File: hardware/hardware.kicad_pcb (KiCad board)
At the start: 2 copper layers, 100 x 100 mm, 129 parts, among them J1 Conn_01x04_Pin, J10 Conn_01x03, J11 AVR-ISP-6, J2 Conn_01x04_Pin, J3 Conn_01x04_Pin, J4 Conn_01x04_Pin, J5 Conn_01x04_Pin, J6 Conn_01x04_Pin, J7 Conn_01x04_Pin, J8 Conn_01x03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

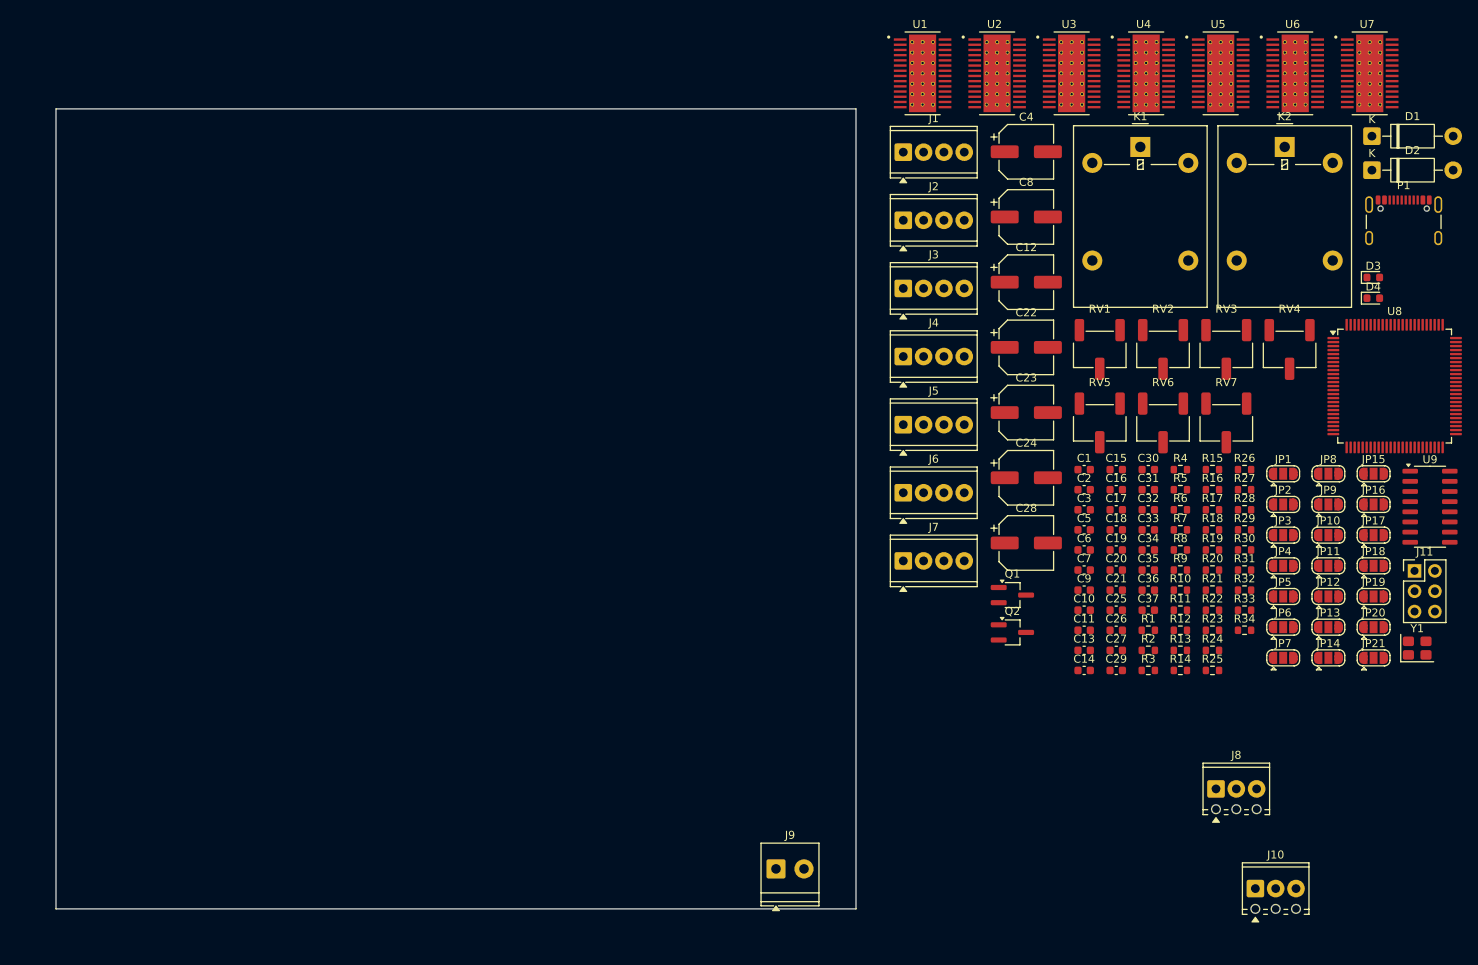
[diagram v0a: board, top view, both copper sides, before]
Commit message: placing relay + drv + edit relay footprints
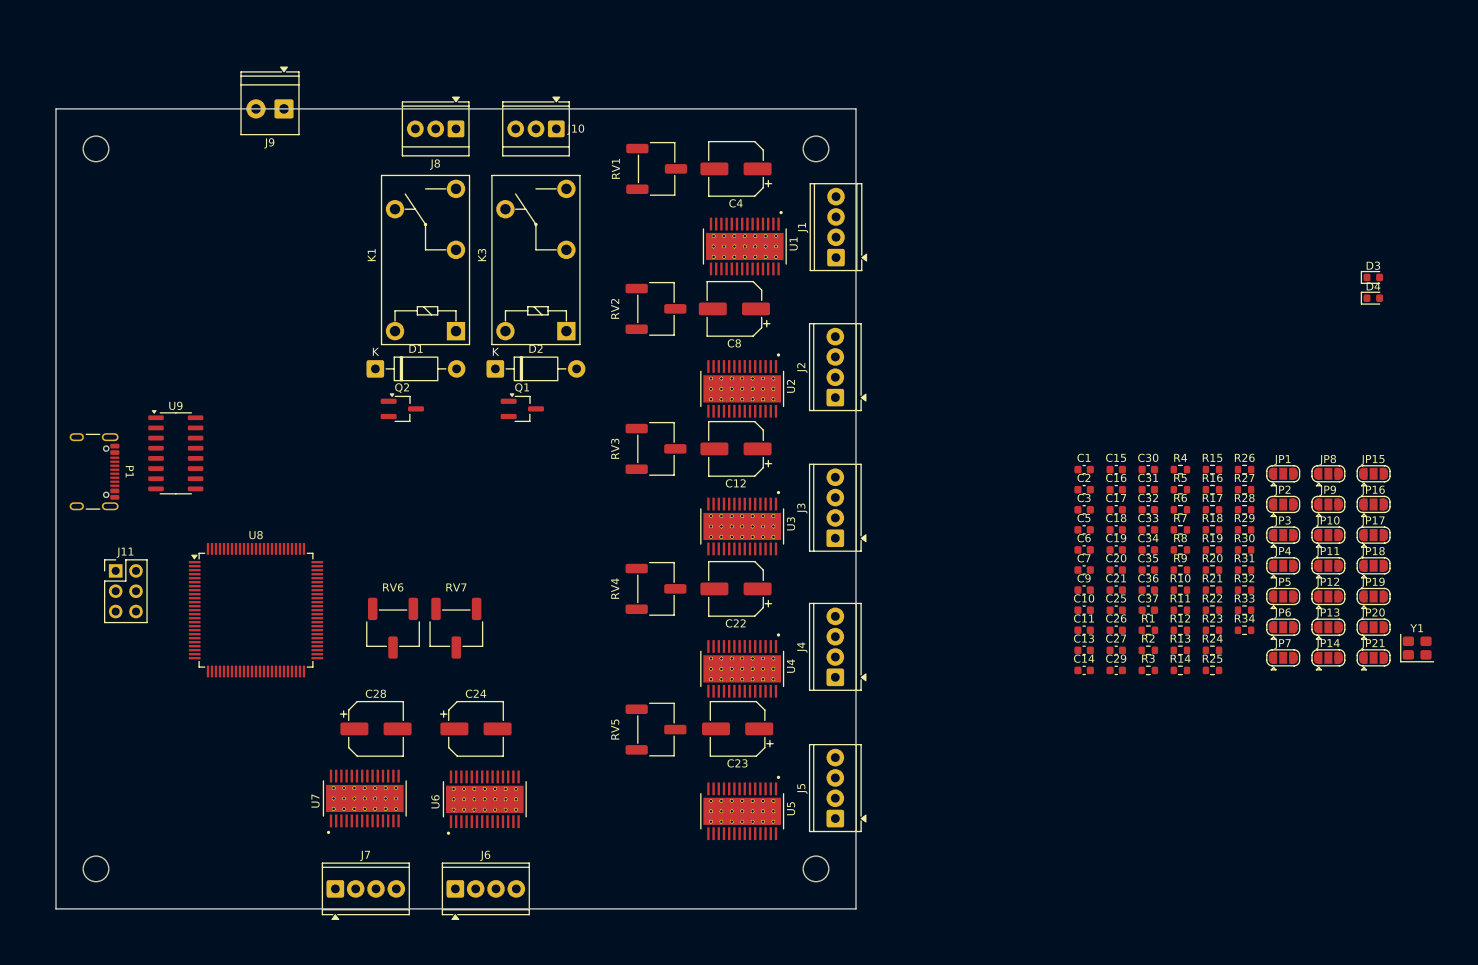
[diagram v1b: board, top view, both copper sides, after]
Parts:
- removed K2: RAYEX-L90, Relay_THT:Relay_SPDT_Omron-G5LE-1
- added K3: G5Q-1, Relay_THT:Relay_SPDT_Omron-G5Q-1, F.Cu at (113.8, 77.8)
- J10, J8: footprint TerminalBlock_Phoenix:TerminalBlock_Phoenix_MPT-0,5-3-2.54_1x03_P2.54mm_Horizontal -> TerminalBlock_TE-Connectivity:TerminalBlock_TE_282834-3_1x03_P2.54mm_Horizontal
- K1: value RAYEX-L90 -> G5Q-1; footprint Relay_THT:Relay_SPDT_Omron-G5LE-1 -> Relay_THT:Relay_SPDT_Omron-G5Q-1
- moved P1 167.5 mm to (53.7, 95.4), turned to -90 degrees
- moved J11 162.4 mm to (57.5, 107.8)
- moved U9 156.9 mm to (65.0, 93.1)
- moved U7 154.9 mm to (88.6, 136.2), turned to 90 degrees
- moved U8 145.1 mm to (75.0, 112.7)
- moved U6 136.0 mm to (103.6, 136.3), turned to 90 degrees
- moved J10 129.0 mm to (112.5, 52.5), turned to 180 degrees
- moved D1 127.9 mm to (89.9, 82.5)
- moved J8 125.8 mm to (100.0, 52.5), turned to 180 degrees
- moved J9 113.2 mm to (78.5, 50.0), turned to 180 degrees
- moved D2 112.4 mm to (104.9, 82.5)
- moved U5 109.9 mm to (135.8, 137.8), turned to -90 degrees
- moved RV6 99.6 mm to (92.1, 114.9)
- moved RV7 99.6 mm to (100.0, 114.9)
- moved U4 90.0 mm to (135.8, 120.0), turned to -90 degrees
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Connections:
- K1 pad 1: (no net) -> Net-(D1-A)
- K1 pad 2: (no net) -> Net-(J8-Pin_2)
- K1 pad 3: (no net) -> Net-(J8-Pin_3)
- K1 pad 4: (no net) -> Net-(J8-Pin_1)
- K1 pad 5: (no net) -> +12V
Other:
- outline, holes or cut-outs redrawn

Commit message: wire all drv
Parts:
- removed R11, R19, R20, R21, R27, R3, R7: 1M, Resistor_SMD:R_0603_1608Metric
- moved D3 150.2 mm to (64.7, 78.6)
- moved D4 150.2 mm to (64.7, 81.2)
- moved Y1 146.8 mm to (73.6, 126.7)
- moved R33 141.6 mm to (60.8, 80.0)
- moved R34 141.6 mm to (60.8, 82.5)
- moved JP19 126.8 mm to (89.2, 129.2)
- moved C31 126.5 mm to (64.2, 130.0)
- moved JP20 126.0 mm to (89.2, 125.8)
- moved JP21 125.6 mm to (89.2, 122.2)
- moved C30 123.1 mm to (69.2, 132.5)
- moved C33 122.9 mm to (64.2, 115.0)
- moved C34 122.9 mm to (64.2, 117.5)
- moved C35 122.9 mm to (64.2, 120.0)
- moved C36 122.9 mm to (64.2, 122.5)
- moved C37 122.9 mm to (64.2, 125.0)
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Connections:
- C11 pad 2: +3.3V -> 3.3_3
- C19 pad 2: +3.3V -> 3.3_4
- C20 pad 2: +3.3V -> 3.3_5
- C21 pad 2: +3.3V -> 3.3_6
- C27 pad 2: +3.3V -> 3.3_7
- C3 pad 2: +3.3V -> 3.3_1
- C7 pad 2: +3.3V -> 3.3_2
- RV1 pad 1: +3.3V -> 3.3_1
- RV2 pad 1: +3.3V -> 3.3_2
- RV3 pad 1: +3.3V -> 3.3_3
- RV4 pad 1: +3.3V -> 3.3_4
- RV5 pad 1: +3.3V -> 3.3_5
- RV6 pad 1: +3.3V -> 3.3_6
- RV7 pad 1: +3.3V -> 3.3_7
- U1 pad 15: +3.3V -> 3.3_1
- U2 pad 15: +3.3V -> 3.3_2
- U3 pad 15: +3.3V -> 3.3_3
- U4 pad 15: +3.3V -> 3.3_4
- U5 pad 15: +3.3V -> 3.3_5
- U6 pad 15: +3.3V -> 3.3_6
- U7 pad 15: +3.3V -> 3.3_7
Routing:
- net +12V: track 0.00 -> 168.6 mm
- net VBUS: track 0.00 -> 159.6 mm
- net Net-(JP3-C): track 0.00 -> 25.4 mm
- net Net-(JP17-C): track 0.00 -> 25.4 mm
- net Net-(JP6-C): track 0.00 -> 25.2 mm
- net Net-(JP16-C): track 0.00 -> 24.9 mm
- net Net-(JP14-C): track 0.00 -> 24.7 mm
- net Net-(JP9-C): track 0.00 -> 24.3 mm
- net Net-(JP18-C): track 0.00 -> 23.9 mm
- net Net-(JP21-C): track 0.00 -> 23.7 mm
- net Net-(JP5-C): track 0.00 -> 22.5 mm
- net Net-(JP2-C): track 0.00 -> 22.4 mm
- net 3.3_5: track 0.00 -> 21.8 mm
- net Net-(JP13-C): track 0.00 -> 21.8 mm
- net Net-(JP8-C): track 0.00 -> 21.5 mm
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
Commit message: finish pcb wiring
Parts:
- added C38: 10u, Capacitor_SMD:C_0603_1608Metric, F.Cu at (79.6, 60.5)
- added C39: 10u, Capacitor_SMD:C_0603_1608Metric, F.Cu at (77.6, 60.5)
- added C40: 0.1µF, Capacitor_SMD:C_0603_1608Metric, F.Cu at (74.1, 56.5)
- added C41: 22u, Capacitor_SMD:C_0603_1608Metric, F.Cu at (64.6, 59.0)
- added C42: 22u, Capacitor_SMD:C_0603_1608Metric, F.Cu at (62.6, 59.0)
- added J12: Conn_01x03, Connector_PinHeader_2.54mm:PinHeader_1x03_P2.54mm_Vertical, F.Cu at (57.6, 62.8)
- added J13: Conn_01x03, Connector_PinHeader_2.54mm:PinHeader_1x03_P2.54mm_Vertical, F.Cu at (57.6, 67.4)
- added J14: Conn_01x03, Connector_PinHeader_2.54mm:PinHeader_1x03_P2.54mm_Vertical, F.Cu at (57.6, 72.0)
- added L2: 4.7uH, Inductor_SMD:L_Chilisin_BMRA00050520, F.Cu at (68.6, 56.5)
- added R3: 10K, Resistor_SMD:R_0603_1608Metric, F.Cu at (69.1, 61.5)
- added R7: 33.0K, Resistor_SMD:R_0603_1608Metric, F.Cu at (71.1, 61.5)
- added REF**: MountingHole_3.2mm_M3_DIN965_Pad, MountingHole:MountingHole_3.2mm_M3_DIN965_Pad, F.Cu at (145.0, 145.0)
- added REF**: MountingHole_3.2mm_M3_DIN965_Pad, MountingHole:MountingHole_3.2mm_M3_DIN965_Pad, F.Cu at (145.0, 55.0)
- added REF**: MountingHole_3.2mm_M3_DIN965_Pad, MountingHole:MountingHole_3.2mm_M3_DIN965_Pad, F.Cu at (55.0, 55.0)
- added REF**: MountingHole_3.2mm_M3_DIN965_Pad, MountingHole:MountingHole_3.2mm_M3_DIN965_Pad, F.Cu at (55.0, 145.0)
- added U10: TPS562200, Package_TO_SOT_SMD:SOT-23-6, F.Cu at (74.1, 59.5)
- Q1, Q2: value Q_NPN -> AO3400A; footprint Package_TO_SOT_SMD:TSOT-23_HandSoldering -> Package_TO_SOT_SMD:SOT-23
- moved C30 28.6 mm to (87.5, 110.5), turned to -45 degrees
- moved C33 27.5 mm to (64.0, 87.5)
- moved R31 27.1 mm to (108.5, 91.5), turned to 180 degrees
- moved R32 26.9 mm to (108.5, 89.5)
- moved C31 23.3 mm to (82.5, 115.5), turned to 135 degrees
- moved Q2 21.9 mm to (108.5, 86.5), turned to 90 degrees
- moved C37 21.5 mm to (64.5, 103.5), turned to 90 degrees
- moved J11 20.1 mm to (73.9, 119.3), turned to -135 degrees
- moved C36 19.2 mm to (66.5, 103.5), turned to 90 degrees
- moved Y1 17.8 mm to (85.0, 113.0), turned to 45 degrees
- moved C32 16.5 mm to (85.5, 96.5), turned to 135 degrees
- moved C35 14.9 mm to (78.5, 115.7), turned to 90 degrees
- moved D3 13.1 mm to (52.5, 83.5)
- moved D4 12.9 mm to (52.5, 85.5)
- moved U8 9.81 mm to (78.5, 103.5), turned to 45 degrees
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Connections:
- net VBUS renamed +5V
- K1 pad 3: Net-(J8-Pin_3) -> Net-(J8-Pin_1)
- K1 pad 4: Net-(J8-Pin_1) -> Net-(J8-Pin_3)
- K3 pad 3: Net-(J10-Pin_3) -> Net-(J10-Pin_1)
- K3 pad 4: Net-(J10-Pin_1) -> Net-(J10-Pin_3)
- Q1 pad 1: (no net) -> Net-(Q1-G)
- Q1 pad 2: (no net) -> GND
- Q1 pad 3: (no net) -> Net-(D1-A)
- Q2 pad 1: (no net) -> Net-(Q2-G)
- Q2 pad 2: (no net) -> GND
- Q2 pad 3: (no net) -> Net-(D2-A)
- R29 pad 1: Net-(Q1-PadB) -> Net-(Q1-G)
- R30 pad 2: Net-(Q1-PadB) -> Net-(Q1-G)
- R31 pad 2: Net-(Q2-PadB) -> Net-(Q2-G)
- R32 pad 1: Net-(Q2-PadB) -> Net-(Q2-G)
- U1 pad 20: DIR -> DIR_1
- U1 pad 22: STEP -> STEP_1
- U2 pad 20: DIR -> DIR_2
- U2 pad 22: STEP -> STEP_2
- U3 pad 20: DIR -> DIR_3
- U3 pad 22: STEP -> STEP_3
- U4 pad 20: DIR -> DIR_4
- U4 pad 22: STEP -> STEP_4
- U5 pad 20: DIR -> DIR_5
- U5 pad 22: STEP -> STEP_5
- U6 pad 20: DIR -> DIR_6
- U6 pad 22: STEP -> STEP_6
- U7 pad 20: DIR -> DIR_7
- U7 pad 22: STEP -> STEP_7
- U8 pad 36: unconnected-(U8-PL1-Pad36) -> STEP_7
- U8 pad 37: unconnected-(U8-PL2-Pad37) -> DIR_7
- U8 pad 38: unconnected-(U8-PL3-Pad38) -> STEP_6
- U8 pad 39: unconnected-(U8-PL4-Pad39) -> DIR_6
- U8 pad 40: unconnected-(U8-PL5-Pad40) -> STEP_5
- U8 pad 41: unconnected-(U8-PL6-Pad41) -> DIR_5
- U8 pad 43: unconnected-(U8-PD0-Pad43) -> SCL
- U8 pad 44: unconnected-(U8-PD1-Pad44) -> SDA
- U8 pad 45: unconnected-(U8-PD2-Pad45) -> RX1
- U8 pad 46: unconnected-(U8-PD3-Pad46) -> TX1
- U8 pad 5: unconnected-(U8-PE3-Pad5) -> SERVO_3
- U8 pad 53: unconnected-(U8-PC0-Pad53) -> STEP_4
- U8 pad 54: unconnected-(U8-PC1-Pad54) -> DIR_4
- U8 pad 55: unconnected-(U8-PC2-Pad55) -> STEP_3
- U8 pad 56: unconnected-(U8-PC3-Pad56) -> DIR_3
- U8 pad 57: unconnected-(U8-PC4-Pad57) -> STEP_2
- U8 pad 58: unconnected-(U8-PC5-Pad58) -> DIR_2
- U8 pad 59: unconnected-(U8-PC6-Pad59) -> STEP_1
- U8 pad 6: unconnected-(U8-PE4-Pad6) -> SERVO_2
- U8 pad 60: unconnected-(U8-PC7-Pad60) -> DIR_1
- U8 pad 7: unconnected-(U8-PE5-Pad7) -> SERVO_1
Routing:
- net +5V: track 159.6 -> 454.8 mm, vias 0 -> 4
- net +12V: track 168.6 -> 410.4 mm
- net STEP_5: track 0.00 -> 70.4 mm, vias 0 -> 2
- net DIR_5: track 0.00 -> 68.6 mm, vias 0 -> 2
- net STEP_1: track 0.00 -> 67.5 mm, vias 0 -> 2
- net DIR_1: track 0.00 -> 66.2 mm, vias 0 -> 2
- net STEP_4: track 0.00 -> 65.2 mm, vias 0 -> 2
- net DIR_4: track 0.00 -> 63.9 mm, vias 0 -> 2
- net STEP_2: track 0.00 -> 55.8 mm, vias 0 -> 2
- net DIR_2: track 0.00 -> 54.8 mm, vias 0 -> 2
- net STEP_3: track 0.00 -> 54.7 mm, vias 0 -> 2
- net DIR_3: track 0.00 -> 53.4 mm, vias 0 -> 2
- net SERVO_1: track 0.00 -> 52.5 mm, vias 0 -> 1
- net RST: track 0.00 -> 49.8 mm, vias 0 -> 2
- net SERVO_2: track 0.00 -> 46.7 mm, vias 0 -> 1
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- added copper zone on B.Cu, net GND
- added copper zone on F.Cu, net GND
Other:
- outline, holes or cut-outs redrawn

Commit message: fix relay +led wiring
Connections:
- U8 pad 71: unconnected-(U8-PA7-Pad71) -> RELAY_1
- U8 pad 72: unconnected-(U8-PA6-Pad72) -> RELAY_2
- U8 pad 77: unconnected-(U8-PA1-Pad77) -> LED1
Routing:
- net RELAY_1: track 0.00 -> 29.8 mm
- net LED1: track 0.00 -> 23.5 mm, vias 0 -> 2
- net RELAY_2: track 0.00 -> 15.0 mm
- net GND: track 29.5 -> 33.3 mm, vias 84 -> 94
- net +5V: track 454.8 -> 457.2 mm
- net DIR_6: track 41.2 -> 42.2 mm
